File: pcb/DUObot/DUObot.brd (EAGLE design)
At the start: 50 x 70 mm, 29 parts, among them U1 MAX3421ESMD, Y1 16MHZ

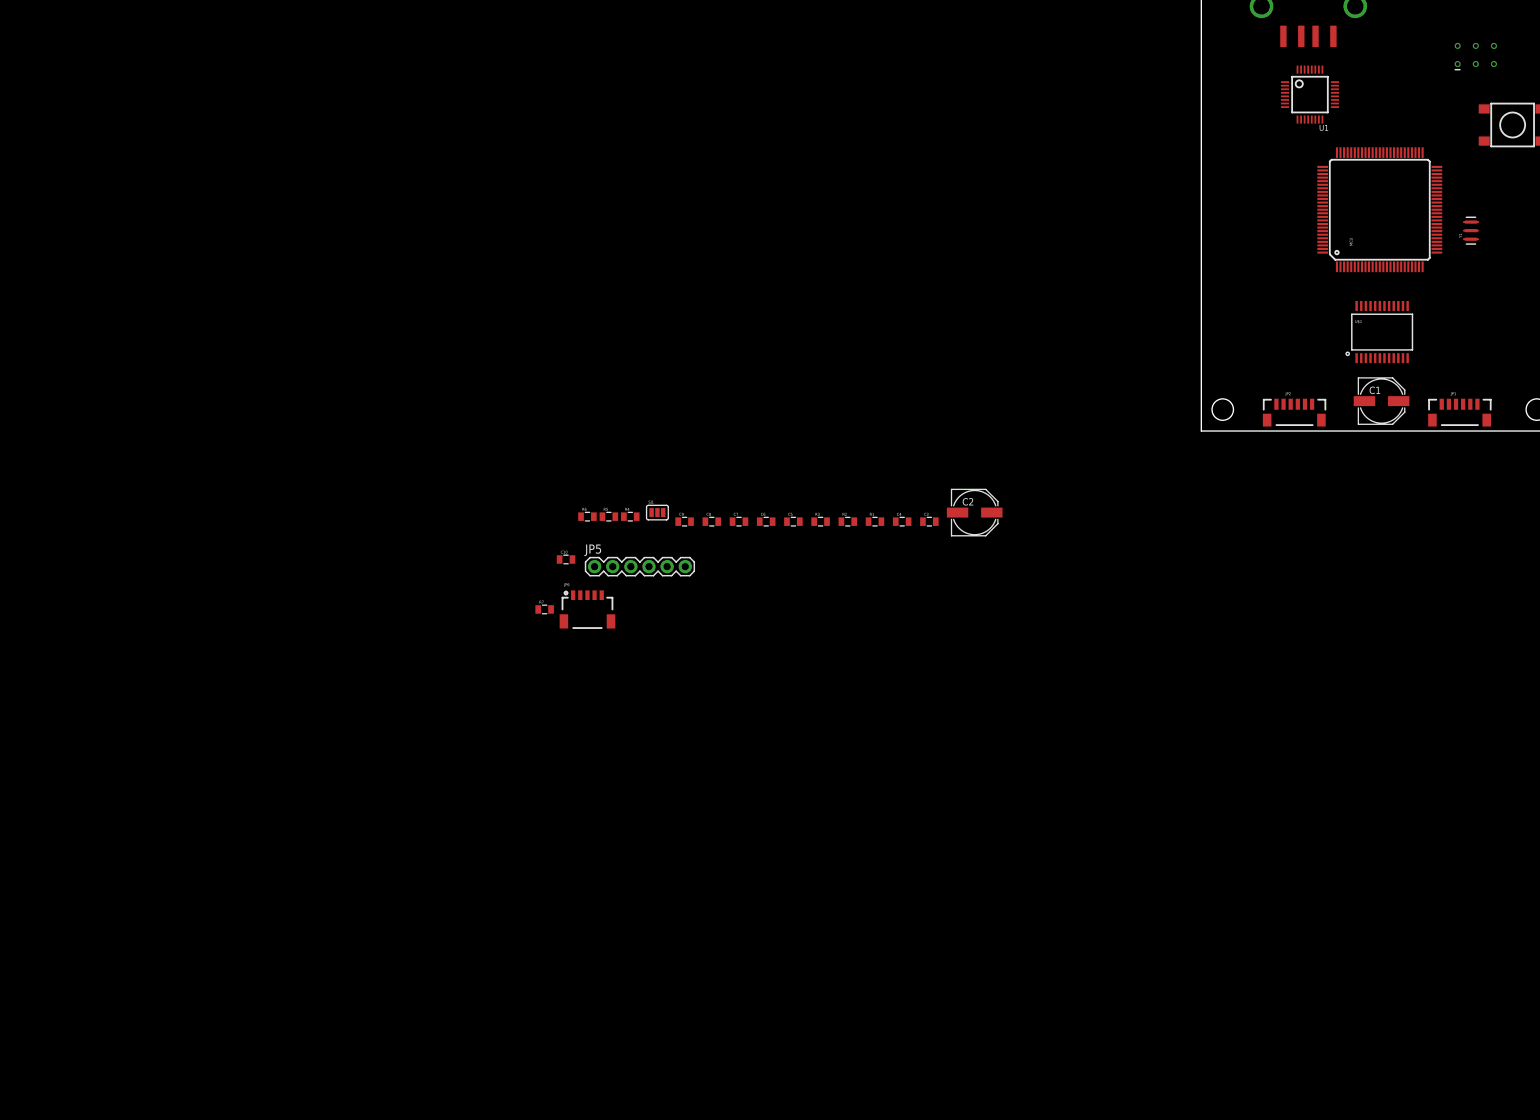
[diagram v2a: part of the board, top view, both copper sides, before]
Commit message: Main board mostly finished - needs minor changes/additions
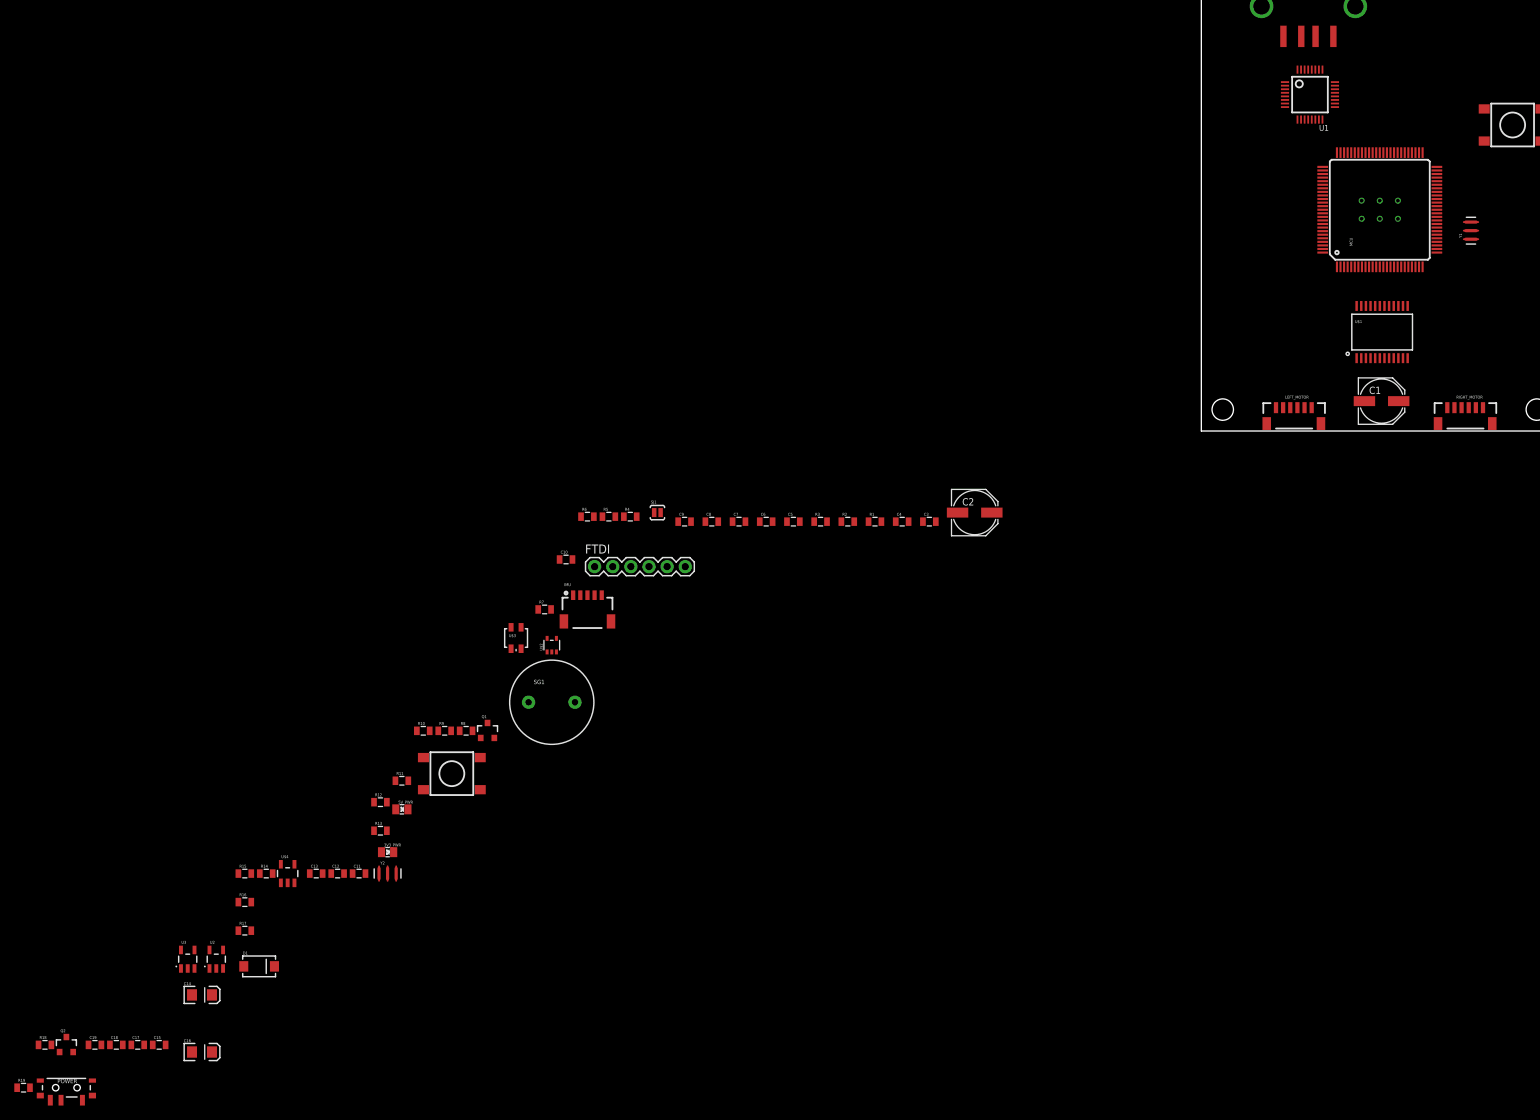
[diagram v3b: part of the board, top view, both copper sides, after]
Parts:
- removed JP1, JP2: (no value), SparkFun-Connectors:1X06-1MM
- removed JP3: AVR_SPI_PRG_6TESTPOINTS, SparkFun-Connectors:2X3_TEST_POINTS
- added 3V3_PWR, 5V_PWR: (no value), SparkFun-LED:LED-0805
- added C11, C12, C13, C15, C17: 0.1u, SparkFun-Passives:0805
- added C14, C16: 10u, SparkFun-Passives:EIA3216
- added C18, C19: 470p, SparkFun-Passives:0805
- added D1: B340A, SparkFun-DiscreteSemi:SMA-DIODE
- added ICSP: (no value), SparkFun-Connectors:2X3_TEST_POINTS
- added LEFT_MOTOR, RIGHT_MOTOR: (no value), SparkFun-Connectors:1X06-1MM
- added POWER: (no value), SparkFun-Electromechanical:SWITCH-SPST-SMD-A
- added Q1, Q2: 200mA/50V, SparkFun-DiscreteSemi:SOT23-3
- added R10, R12, R13, R8, R9: (no value), SparkFun-Passives:0805
- added R11, R14, R15, R17: 10k, SparkFun-Passives:0805
- added R16, R18, R19: 20k, SparkFun-Passives:0805
- added S2: (no value), SparkFun-Electromechanical:TACTILE_SWITCH_TALL
- added SG1: BUZZERPTH-KIT, SparkFun-Electromechanical:BUZZER-12MM-KIT
- added U$2: 74AHC1G08, SparkFun-DigitalIC:SOT353
- added U$3: LED-TRICOLOR, SparkFun-LED:LED-TRICOLOR-SMD
- added U$4: MCP6021T-E/OT, SparkFun-AnalogIC:SOT23-5
- added U2: MIC5219 5V, SparkFun-PowerIC:SOT23-5
- added U3: 3.3V/150mA, SparkFun-PowerIC:SOT23-5
- added Y2: 12MHZ, SparkFun-FreqCtrl:RESONATOR-SMD
- C2: value (none) -> 47u
- SJ1: value JUMPER-PAD-3-NOYES_SILK -> JUMPER-PAD-2-NOYES_SILK; device SparkFun-Passives:PAD-JUMPER-3-NO_YES_SILK -> SparkFun-Passives:PAD-JUMPER-2-NO_YES_SILK
- USB: value USB-A-SMD -> (none)
- renumbered JP4 to USB, JP5 to FTDI, JP6 to IMU
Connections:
- net N$11 renamed U_INT
- new net BATT_LVL: MCU.82, R16.1, R17.2
- new net BUZZER: MCU.1, Q1.1
- new net B_LED: MCU.5, R9.1
- new net GPIO1: MCU.89
- new net GPIO2: MCU.88
- new net GPIO3: MCU.87
- new net GPIO4: MCU.86
- new net GPIO5: MCU.85
- new net GPIO6: MCU.84
- new net GPIO7: MCU.83
- new net G_LED: MCU.6, R10.1
- new net INT6: MCU.8
- new net INT7: MCU.9, R11.1, S2.B2
- new net N$11: R14.1, R15.2, U$4.3
- new net N$12: U$1.19, U$2.4
- new net N$13: Q1.3, SG1.-
- new net N$14: R9.2, U$3.B
- new net N$15: R8.2, U$3.R
- new net N$16: R10.2, U$3.G
- new net N$17: 5V_PWR.ANODE, R12.1
- new net N$18: 3V3_PWR.ANODE, R13.1
- new net N$19: U1.25, Y2.1
- new net N$20: U1.24, Y2.3
- new net N$21: C19.1, U2.4
- new net N$22: C18.1, U3.4
- new net N$23: U$4.2
- new net N$24: U$4.5
- new net N$25: D1.C, Q2.3
- new net N$27: POWER.1, R19.2
- new net N$28: POWER.3, R18.1
- new net N$29: POWER.2, Q2.1
- new net PWM1: MCU.15
- new net PWM2: MCU.16
- new net PWM3: MCU.17
- new net R_LED: MCU.7, R8.1
- new net U_MISO: U1.15
- new net U_MOSI: U1.16
- new net U_RES: U1.12
- new net U_SCK: U1.13
- new net U_SS: U1.14
- new net V_BATT: D1.A, R18.2
- new net V_COMP: U$2.1, U$4.1
- net 3.3V: now also C11.1, C12.1, C14.A, C17.1, R13.2, SJ1.2, U$4.4, U3.5; no longer SJ1.1
- net 5V: now also C13.1, C15.1, C16.A, ICSP.2, LEFT_MOTOR.4, R11.2, R12.2, RIGHT_MOTOR.4, SG1.+, U$2.5, U$3.A, U2.5, U3.1, U3.3; no longer JP1.4, JP2.4, JP3.2, SJ1.3
- net AREF: now also SJ1.1; no longer SJ1.2
- net GND: now also 3V3_PWR.CATHODE, 5V_PWR.CATHODE, C11.2, C12.2, C13.2, C14.C, C15.2, C16.C, C17.2, C18.2, C19.2, C2.-, C4.2, ICSP.6, LEFT_MOTOR.1, Q1.2, R15.1, R17.1, R19.1, RIGHT_MOTOR.1, S2.A2, U$2.3, U2.2, U3.2, Y2.2; no longer JP1.1, JP2.1, JP3.6
- net LENCA: now also LEFT_MOTOR.3; no longer JP1.3
- net LENCB: now also LEFT_MOTOR.2; no longer JP1.2
- net MISO: now also ICSP.1; no longer JP3.1
- net MOSI: now also ICSP.4; no longer JP3.4
- net N$1: now also RIGHT_MOTOR.5; no longer JP2.5
- net N$2: now also RIGHT_MOTOR.6; no longer JP2.6
- net N$3: now also LEFT_MOTOR.6; no longer JP1.6
- net N$4: now also LEFT_MOTOR.5; no longer JP1.5
- net RENCA: now also RIGHT_MOTOR.3; no longer JP2.3
- net RENCB: now also RIGHT_MOTOR.2; no longer JP2.2
- net RESET: now also ICSP.5; no longer JP3.5
- net SCK: now also ICSP.3; no longer JP3.3
- net SCL: no longer IMU.5, R3.1
- net SDA: no longer IMU.4, R2.1
- net STBY: now also U$2.2; no longer U$1.19
- net VCC: now also C2.+, C4.1, Q2.2, R14.2, R16.2, U2.1, U2.3

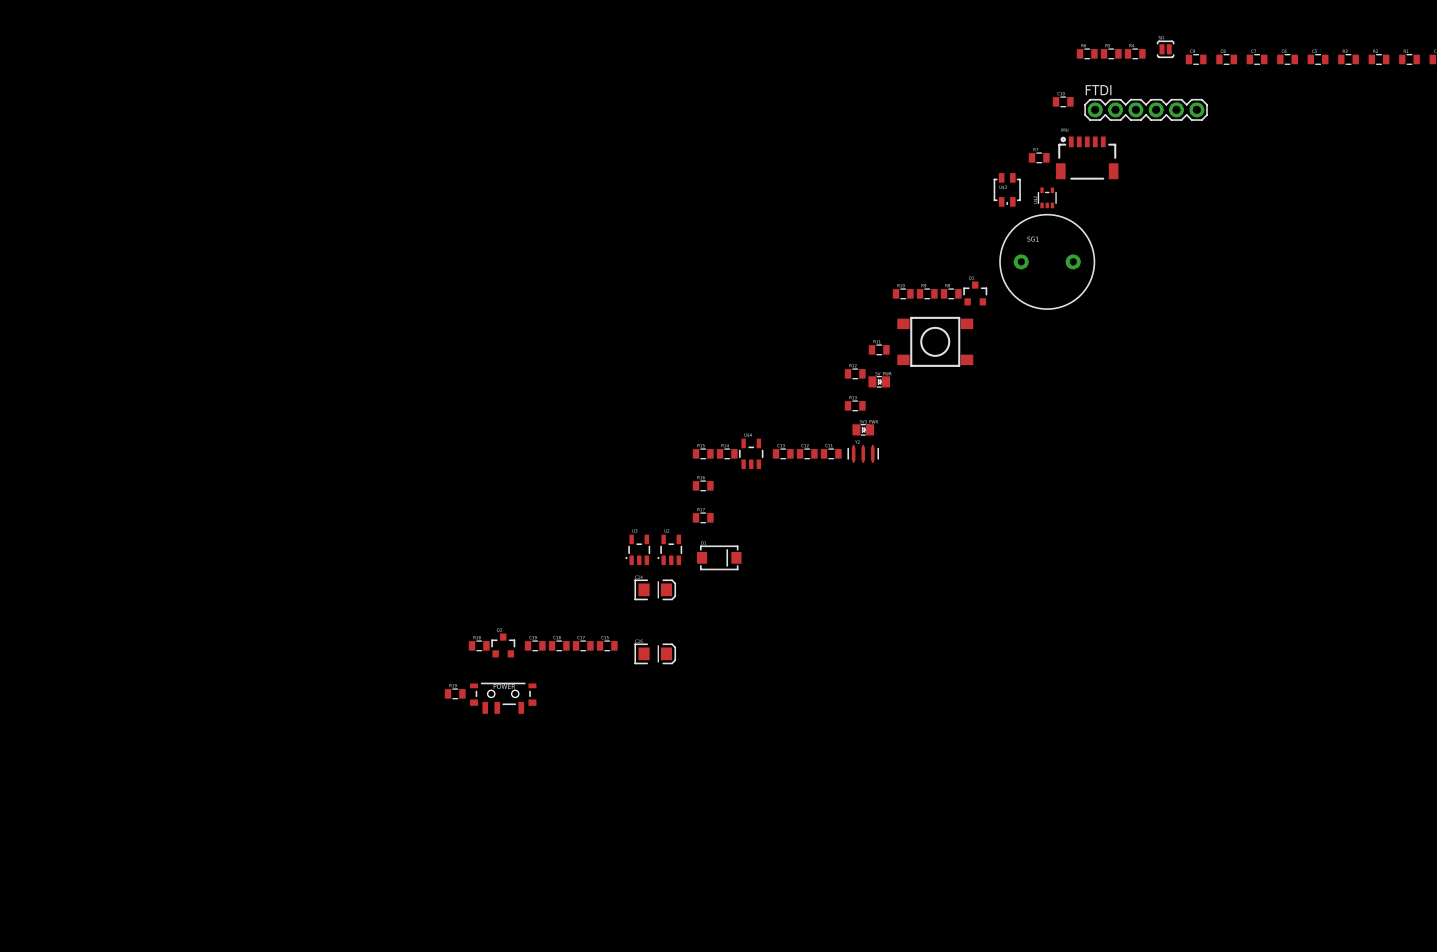
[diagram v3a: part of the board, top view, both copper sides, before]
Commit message: Change individual pull-up resistors to arrays
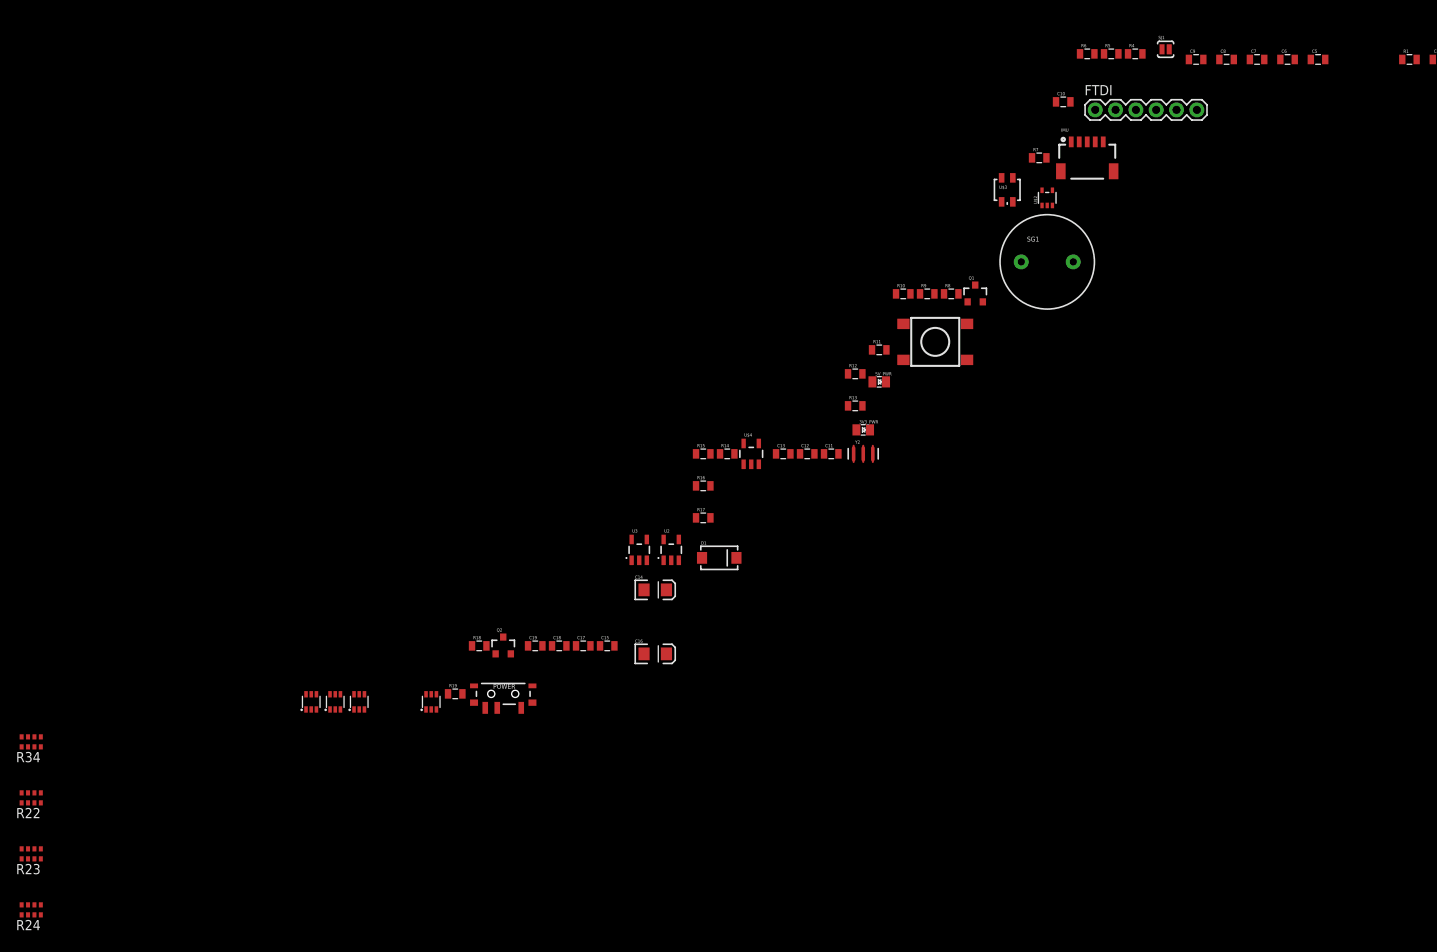
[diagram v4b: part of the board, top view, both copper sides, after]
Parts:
- removed R2, R3: 10k, SparkFun-Passives:0805
- added R22, R23, R24, R34: (no value), SparkFun-Resistors:0603-ARV
- added U$5, U$6, U$7, U$8: MOSFET, SparkFun-DiscreteSemi:SOT363_V2
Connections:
- new net N$32: IMU.4, R24.3, U$5.S1
- new net N$33: IMU.5, R24.4, U$5.S2
- new net N$37: R23.2, U$6.D1
- new net N$38: R23.1, U$6.D2
- net 3.3V: now also R22.5, R22.6, R22.7, R22.8, R23.5, R23.6, R24.5, R24.6, U$5.G1, U$5.G2, U$6.G1, U$6.G2, U$7.G1, U$7.G2, U$8.G1, U$8.G2
- net 5V: now also R23.7, R23.8, R24.7, R24.8, R34.5, R34.6, R34.7, R34.8; no longer R2.2, R3.2
- net MISO: now also R34.2, U$7.D2
- net MOSI: now also R34.1, U$7.D1
- net SCK: now also R34.4, U$8.D1
- net SCL: now also R24.1, U$5.D2
- net SDA: now also R24.2, U$5.D1
- net SS: now also R34.3, U$8.D2
- net U_INT: now also R23.4, U$6.S1
- net U_MISO: now also R22.3, U$7.S2
- net U_MOSI: now also R22.4, U$7.S1
- net U_RES: now also R23.3, U$6.S2
- net U_SCK: now also R22.2, U$8.S1
- net U_SS: now also R22.1, U$8.S2
